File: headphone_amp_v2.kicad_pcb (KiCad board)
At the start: 2 copper layers, 72 parts, among them J1 USB_OTG, J2 HID_JMP, J3 AudioJack3_Ground, U1 PCM2707PJTG4, U2 PCM1794A, U3 TPS60501DGS, U4 SMDIP-8_W7.62mm, U5 SMDIP-8_W7.62mm, U6 LM2662M, Y1 12Mhz

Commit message: updated board layout as suggested by the reddit community. New rendered pictures added. Polyfuse for VBUS added
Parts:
- removed the REF** at (29.2, 19.1)
- removed the REF** at (102.9, 19.1)
- removed the REF** at (102.9, 81.3)
- removed the REF** at (29.2, 81.3)
- added C17: 10uF, Capacitors_SMD:CP_Elec_5x5.3, F.Cu at (39.8, 76.6)
- added F1: Polyfuse, Fuse_Holders_and_Fuses:Fuse_SMD1206_HandSoldering, F.Cu at (64.0, 25.0)
- added REF**: MountingHole_3.2mm_M3, Mounting_Holes:MountingHole_3.2mm_M3, F.Cu at (103.5, 18.5)
- added REF**: MountingHole_3.2mm_M3, Mounting_Holes:MountingHole_3.2mm_M3, F.Cu at (103.5, 79.0)
- added REF**: MountingHole_3.2mm_M3, Mounting_Holes:MountingHole_3.2mm_M3, F.Cu at (28.5, 79.0)
- added REF**: MountingHole_3.2mm_M3, Mounting_Holes:MountingHole_3.2mm_M3, F.Cu at (28.5, 18.5)
- U4, U5: value SMDIP-8_W7.62mm -> OPA2134PA
- moved C23 71.6 mm to (74.9, 74.0), turned to 90 degrees
- moved R16 68.6 mm to (79.4, 69.4)
- moved C26 68.3 mm to (84.0, 73.3), turned to 270 degrees
- moved R14 66.5 mm to (79.5, 72.7)
- moved C28 66.5 mm to (84.1, 66.2), turned to 270 degrees
- moved R18 64.8 mm to (79.3, 65.6)
- moved R20 63.7 mm to (79.3, 59.8)
- moved C22 58.0 mm to (75.0, 61.0), turned to 270 degrees
- moved C30 46.8 mm to (75.4, 33.4)
- moved U6 46.4 mm to (73.8, 25.1)
- moved C19 45.4 mm to (29.8, 58.5), turned to 180 degrees
- moved C31 44.5 mm to (78.8, 17.8)
- moved U3 41.8 mm to (29.8, 64.4), turned to 90 degrees
- moved C20 41.7 mm to (29.8, 70.0), turned to 180 degrees
- moved U4 27.1 mm to (91.3, 71.1)
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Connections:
- C8 pad 2: Net-(C8-Pad2) -> 5V
- J1 pad 1: 5V -> Net-(F1-Pad1)
- L1 pad 1: 5V -> Net-(F1-Pad2)
- L1 pad 2: Net-(C8-Pad2) -> 5V
- U1 pad 24: Net-(C8-Pad2) -> 5V
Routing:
- net 5V: track 35.0 -> 234.3 mm, vias 1 -> 9
- net -5V: track 7.39 -> 77.3 mm, vias 0 -> 3
- net 3.3V: track 3.64 -> 40.4 mm
- net OUTL: track 1.00 -> 33.3 mm, vias 0 -> 2
- net IOUTR-: track 0.00 -> 31.0 mm, vias 0 -> 2
- net IOUTR+: track 0.00 -> 28.4 mm
- net IOUTL+: track 0.00 -> 20.2 mm, vias 0 -> 2
- net IOUTL-: track 0.00 -> 18.2 mm
- net OUTR: track 4.31 -> 21.5 mm
- net Net-(C2-Pad1): track 8.61 -> 20.9 mm, vias 0 -> 4
- net Net-(C29-Pad1): track 20.9 -> 33.1 mm, vias 1 -> 0
- net Net-(C28-Pad1): track 24.4 -> 36.6 mm
- net Net-(C10-Pad2): track 0.00 -> 11.2 mm
- net Net-(C9-Pad2): track 0.00 -> 10.4 mm
- net GND: track 51.8 -> 61.6 mm, vias 11 -> 40
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
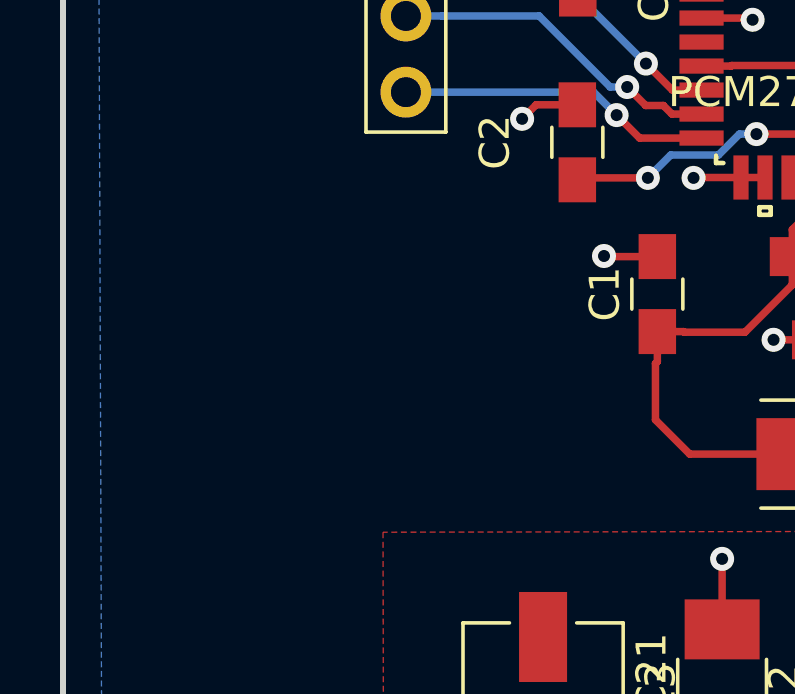
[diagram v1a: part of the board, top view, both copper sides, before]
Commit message: minor changes, HMTL BOM created
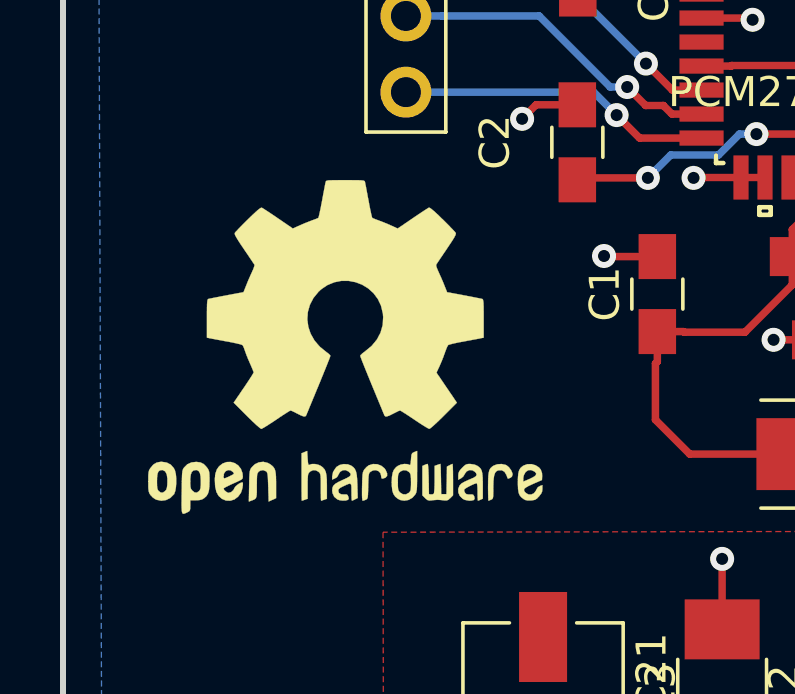
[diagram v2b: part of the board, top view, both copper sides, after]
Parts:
- added REF***: OSHW-Logo2_14.6x12mm_SilkScreen, Symbols:OSHW-Logo2_14.6x12mm_SilkScreen, F.Cu at (31.0, 41.5)

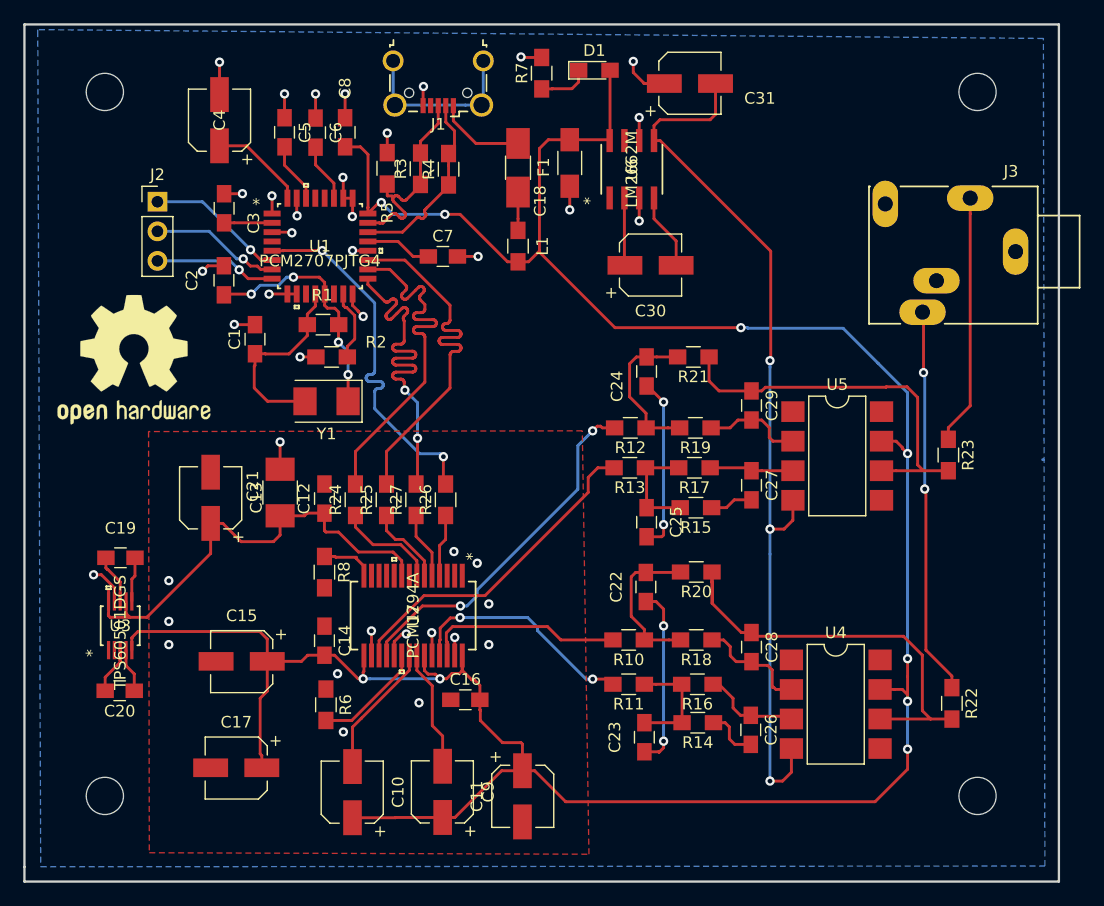
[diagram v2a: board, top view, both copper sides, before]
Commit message: fixed some footprints, inserted all needed specification sheets, updated the BOM list
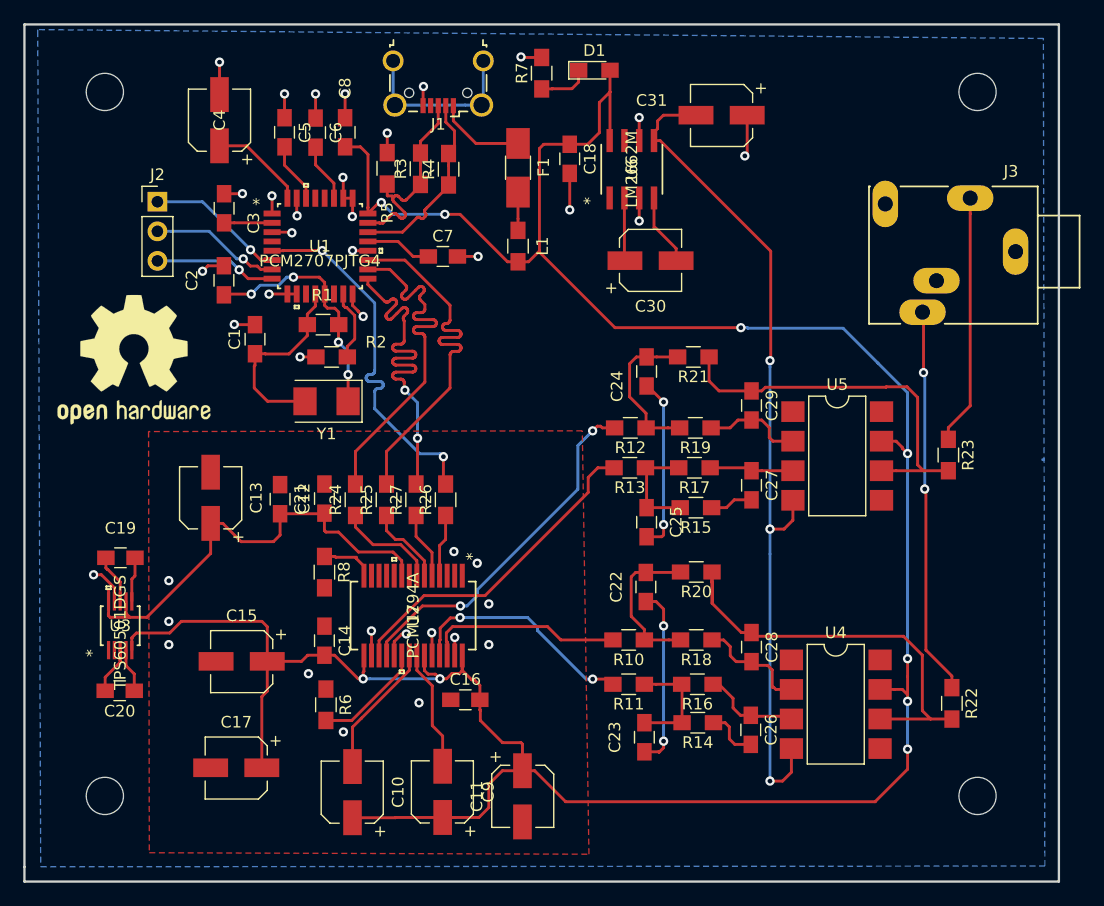
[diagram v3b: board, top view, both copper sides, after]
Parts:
- C18: footprint Capacitors_SMD:C_1206_HandSoldering -> Capacitors_SMD:C_0805_HandSoldering
- C21: footprint Capacitors_SMD:C_1210_HandSoldering -> Capacitors_SMD:C_0805_HandSoldering
- moved C31 3.85 mm to (81.5, 20.5), turned to 180 degrees
- moved C21 0.57 mm to (43.6, 53.5)
- moved C30 0.40 mm to (75.4, 33.0)
- moved C18 0.36 mm to (68.5, 24.2)
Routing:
- net 5V: track 234.3 -> 241.1 mm
- net -5V: track 77.3 -> 73.0 mm
- net GND: track 61.6 -> 59.9 mm, vias 40 -> 39
